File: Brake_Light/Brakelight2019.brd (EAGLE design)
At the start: 62.2 x 38.1 mm, 62 parts, among them J1 POWER_JACK, U1 R-78E5.0-1.0

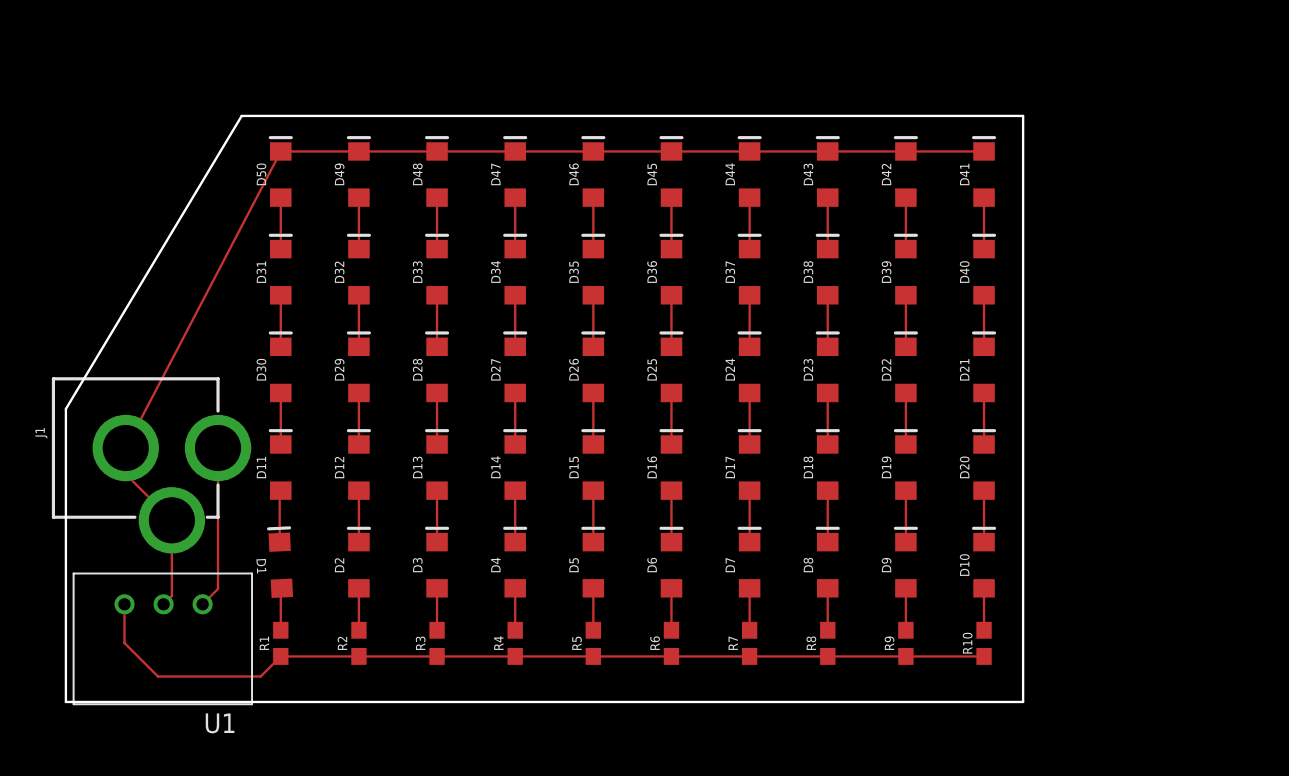
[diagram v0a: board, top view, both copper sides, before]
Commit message: Add files via upload
changed out LEDs and voltage regulator for better ones.
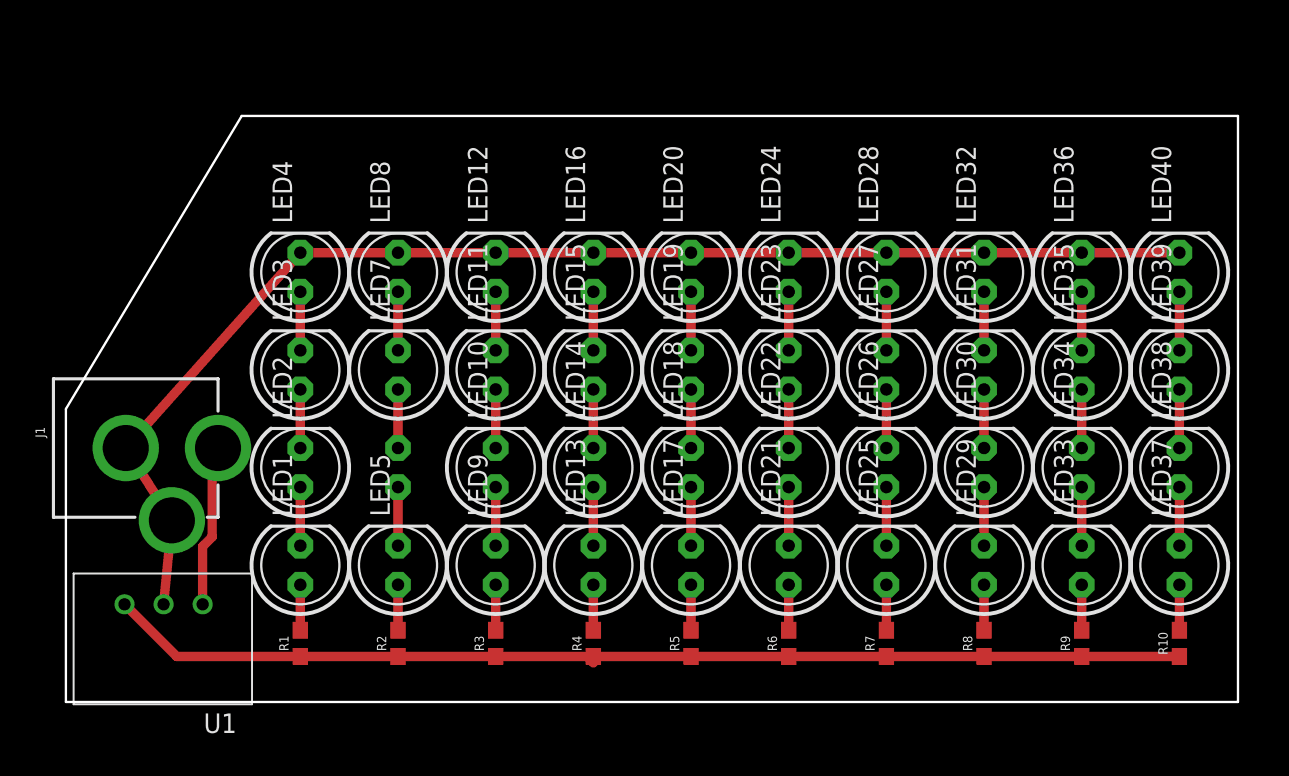
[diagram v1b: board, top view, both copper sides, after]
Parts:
- removed D1, D10, D11, D12, D13, D14, D15, D16, D17, D18, D19, D2, D20, D21, D22, D23, D24, D25, D26, D27, D28, D29, D3, D30, D31, D32, D33, D34, D35, D36, D37, D38, D39, D4, D40, D41, D42, D43, D44, D45, D46, D47, D48, D49, D5, D50, D6, D7, D8, D9: RED, SparkFun-LED:LED-1206
- added LED1, LED10, LED11, LED12, LED13, LED14, LED15, LED16, LED17, LED18, LED19, LED2, LED20, LED21, LED22, LED23, LED24, LED25, LED26, LED27, LED28, LED29, LED3, LED30, LED31, LED32, LED33, LED34, LED35, LED36, LED37, LED38, LED39, LED4, LED40, LED5, LED6, LED7, LED8, LED9: (no value), adafruit:LED5MM
- moved R10 12.7 mm to (77.5, 3.81)
- moved R9 11.4 mm to (71.1, 3.81)
- moved R8 10.2 mm to (64.8, 3.81)
- moved R7 8.89 mm to (58.4, 3.81)
- moved R6 7.62 mm to (52.1, 3.81)
- moved R5 6.35 mm to (45.7, 3.81)
- moved R4 5.08 mm to (39.4, 3.81)
- moved R3 3.81 mm to (33.0, 3.81)
- moved R2 2.54 mm to (26.7, 3.81)
- moved R1 1.27 mm to (20.3, 3.81)
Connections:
- removed net N$41: D1.A, R1.2
- removed net N$42: D2.A, R2.2
- removed net N$43: D3.A, R3.2
- removed net N$44: D4.A, R4.2
- removed net N$45: D5.A, R5.2
- removed net N$46: D6.A, R6.2
- removed net N$47: D7.A, R7.2
- removed net N$48: D8.A, R8.2
- removed net N$49: D9.A, R9.2
- removed net N$50: D10.A, R10.2
- net GND: now also LED12.K, LED16.K, LED20.K, LED24.K, LED28.K, LED32.K, LED36.K, LED4.K, LED40.K, LED8.K; no longer D41.C, D42.C, D43.C, D44.C, D45.C, D46.C, D47.C, D48.C, D49.C, D50.C
- net N$1: now also LED1.A, R1.2; no longer D1.C, D11.A
- net N$10: now also LED10.A, LED9.K; no longer D10.C, D20.A
- net N$11: now also LED10.K, LED11.A; no longer D20.C, D21.A
- net N$12: now also LED11.K, LED12.A; no longer D19.C, D22.A
- net N$13: now also LED13.A, R4.2; no longer D18.C, D23.A
- net N$14: now also LED13.K, LED14.A; no longer D17.C, D24.A
- net N$15: now also LED14.K, LED15.A; no longer D16.C, D25.A
- net N$16: now also LED15.K, LED16.A; no longer D15.C, D26.A
- net N$17: now also LED17.A, R5.2; no longer D14.C, D27.A
- net N$18: now also LED17.K, LED18.A; no longer D13.C, D28.A
- net N$19: now also LED18.K, LED19.A; no longer D12.C, D29.A
- net N$2: now also LED1.K, LED2.A; no longer D12.A, D2.C
- net N$20: now also LED19.K, LED20.A; no longer D11.C, D30.A
- net N$21: now also LED21.A, R6.2; no longer D30.C, D31.A
- net N$22: now also LED21.K, LED22.A; no longer D29.C, D32.A
- net N$23: now also LED22.K, LED23.A; no longer D28.C, D33.A
- net N$24: now also LED23.K, LED24.A; no longer D27.C, D34.A
- net N$25: now also LED25.A, R7.2; no longer D26.C, D35.A
- net N$26: now also LED25.K, LED26.A; no longer D25.C, D36.A
- net N$27: now also LED26.K, LED27.A; no longer D24.C, D37.A
- net N$28: now also LED27.K, LED28.A; no longer D23.C, D38.A
- net N$29: now also LED29.A, R8.2; no longer D22.C, D39.A
- net N$3: now also LED2.K, LED3.A; no longer D13.A, D3.C
- net N$30: now also LED29.K, LED30.A; no longer D21.C, D40.A
- net N$31: now also LED30.K, LED31.A; no longer D40.C, D41.A
- net N$32: now also LED31.K, LED32.A; no longer D39.C, D42.A
- net N$33: now also LED33.A, R9.2; no longer D38.C, D43.A
- net N$34: now also LED33.K, LED34.A; no longer D37.C, D44.A
- net N$35: now also LED34.K, LED35.A; no longer D36.C, D45.A
- net N$36: now also LED35.K, LED36.A; no longer D35.C, D46.A
- net N$37: now also LED37.A, R10.2; no longer D34.C, D47.A
- net N$38: now also LED37.K, LED38.A; no longer D33.C, D48.A
- net N$39: now also LED38.K, LED39.A; no longer D32.C, D49.A
- net N$4: now also LED3.K, LED4.A; no longer D14.A, D4.C
- net N$40: now also LED39.K, LED40.A; no longer D31.C, D50.A
- net N$5: now also LED5.A, R2.2; no longer D15.A, D5.C
- net N$6: now also LED5.K, LED6.A; no longer D16.A, D6.C
- net N$7: now also LED6.K, LED7.A; no longer D17.A, D7.C
- net N$8: now also LED7.K, LED8.A; no longer D18.A, D8.C
- net N$9: now also LED9.A, R3.2; no longer D19.A, D9.C
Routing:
- net 5V: track 59.8 -> 70.2 mm
- net GND: track 79.1 -> 85.2 mm
- net N$41: track 2.76 -> 0.00 mm
- net N$50: track 2.73 -> 0.00 mm
- net N$49: track 2.73 -> 0.00 mm
- net N$48: track 2.73 -> 0.00 mm
- net N$47: track 2.73 -> 0.00 mm
- net N$46: track 2.73 -> 0.00 mm
- net N$45: track 2.73 -> 0.00 mm
- net N$44: track 2.73 -> 0.00 mm
- net N$43: track 2.73 -> 0.00 mm
- net N$42: track 2.73 -> 0.00 mm
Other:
- board size 62.2 x 38.1 mm -> 76.2 x 38.1 mm

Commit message: Add files via upload
Here you go tony
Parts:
- added 5V_BYPASS: (no value), SparkFun-Connectors:1X02
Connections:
- net 5V: now also 5V_BYPASS.1
- net GND: now also 5V_BYPASS.2
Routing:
- net GND: track 85.2 -> 94.9 mm
- net 5V: track 70.2 -> 73.8 mm
- added copper zone on layer 1, net 5V
- added copper zone on layer 16, net GND
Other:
- board size 76.2 x 38.1 mm -> 77.5 x 33 mm
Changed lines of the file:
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@@
 <board>
 <plain>
-<wire x1="5.08" y1="0" x2="81.28" y2="0" width="0.1524" layer="20"/>
-<wire x1="81.28" y1="0" x2="81.28" y2="38.1" width="0.1524" layer="20"/>
-<wire x1="81.28" y1="38.1" x2="16.51" y2="38.1" width="0.1524" layer="20"/>
-<wire x1="16.51" y1="38.1" x2="5.08" y2="19.05" width="0.1524" layer="20"/>
+<wire x1="5.08" y1="0" x2="82.55" y2="0" width="0.1524" layer="20"/>
+<wire x1="82.55" y1="0" x2="82.55" y2="33.02" width="0.1524" layer="20"/>
+<wire x1="82.55" y1="33.02" x2="5.08" y2="33.02" width="0.1524" layer="20"/>
+<wire x1="5.08" y1="33.02" x2="5.08" y2="19.05" width="0.1524" layer="20"/>
 <wire x1="5.08" y1="19.05" x2="5.08" y2="0" width="0.1524" layer="20"/>
 <dimension x1="17.78" y1="31.75" x2="80.01" y2="40.64" x3="48.895" y3="41.91" textsize="1.778" layer="1" dtype="horizontal"/>
 <dimension x1="83.82" y1="30.48" x2="100.33" y2="6.35" x3="100.33" y3="18.415" textsize="1.778" layer="1" dtype="vertical"/>
+<hole x="6.858" y="31.496" drill="1"/>
+<hole x="15.24" y="31.496" drill="1"/>
+<hole x="6.858" y="22.86" drill="1"/>
+<hole x="81.28" y="1.27" drill="1"/>
+<hole x="6.35" y="1.27" drill="1"/>
+<hole x="41.91" y="1.016" drill="1"/>
+<hole x="81.28" y="31.75" drill="1"/>
+<hole x="41.91" y="31.75" drill="1"/>
+<hole x="60.96" y="31.75" drill="1"/>
+<hole x="60.96" y="1.016" drill="1"/>
+<hole x="28.194" y="31.75" drill="1"/>
+<hole x="28.448" y="1.016" drill="1"/>
+<hole x="81.28" y="17.78" drill="1"/>
 </plain>
 <attributes>
@@
 <element name="LED39" library="adafruit" library_urn="urn:adsk.eagle:library:420" package="LED5MM" package3d_urn="urn:adsk.eagle:package:6240538/1" value="" x="77.47" y="21.59" rot="R90"/>
 <element name="LED40" library="adafruit" library_urn="urn:adsk.eagle:library:420" package="LED5MM" package3d_urn="urn:adsk.eagle:package:6240538/1" value="" x="77.47" y="27.94" rot="R90"/>
+<element name="5V_BYPASS" library="SparkFun-Connectors" library_urn="urn:adsk.eagle:library:513" package="1X02" package3d_urn="urn:adsk.eagle:package:38039/1" value="" x="11.938" y="2.032" rot="R180"/>
 </elements>
 <signals>
@@
 <wire x1="20.32" y1="29.21" x2="8.97" y2="16.51" width="0.6096" layer="1"/>
 <wire x1="8.97" y1="16.51" x2="11.97" y2="11.81" width="0.6096" layer="1"/>
-<wire x1="11.97" y1="11.81" x2="11.43" y2="6.35" width="0.6096" layer="1"/>
+<wire x1="11.97" y1="11.81" x2="11.556846875" y2="7.632575" width="0.6096" layer="1"/>
+<contactref element="5V_BYPASS" pad="2"/>
+<wire x1="11.556846875" y1="7.632575" x2="11.43" y2="6.35" width="0.6096" layer="1"/>
+<wire x1="9.398" y1="2.032" x2="9.398" y2="2.22436875" width="0.6096" layer="1"/>
+<wire x1="9.398" y1="2.22436875" x2="7.708" y2="3.91436875" width="0.6096" layer="1"/>
+<wire x1="7.708" y1="3.91436875" x2="7.708" y2="6.739475" width="0.6096" layer="1"/>
+<wire x1="7.708" y1="6.739475" x2="8.429725" y2="7.4612" width="0.6096" layer="1"/>
+<wire x1="11.385471875" y1="7.4612" x2="11.556846875" y2="7.632575" width="0.6096" layer="1"/>
+<wire x1="8.429725" y1="7.4612" x2="11.385471875" y2="7.4612" width="0.6096" layer="1"/>
+<polygon width="0.6096" layer="16">
+<vertex x="5.08" y="33.02"/>
+<vertex x="5.08" y="0"/>
+<vertex x="82.55" y="0"/>
+<vertex x="82.55" y="33.02"/>
+</polygon>
 </signal>
 <signal name="5V">
@@
 <contactref element="R9" pad="1"/>
 <contactref element="R10" pad="1"/>
-<wire x1="20.32" y1="2.96" x2="12.28" y2="2.96" width="0.6096" layer="1"/>
-<wire x1="12.28" y1="2.96" x2="8.89" y2="6.35" width="0.6096" layer="1"/>
+<wire x1="19.05" y1="4.23" x2="12.192" y2="4.23" width="0.6096" layer="1"/>
+<wire x1="12.192" y1="4.23" x2="8.978" y2="4.23" width="0.6096" layer="1"/>
+<wire x1="8.978" y1="4.23" x2="8.89" y2="4.142" width="0.6096" layer="1"/>
 <wire x1="20.32" y1="2.96" x2="26.67" y2="2.96" width="0.6096" layer="1"/>
 <wire x1="26.67" y1="2.96" x2="33.02" y2="2.96" width="0.6096" layer="1"/>
@@
 <wire x1="64.77" y1="2.96" x2="71.12" y2="2.96" width="0.6096" layer="1"/>
 <wire x1="71.12" y1="2.96" x2="77.47" y2="2.96" width="0.6096" layer="1"/>
-<wire x1="38.95" y1="2.96" x2="39.37" y2="2.96" width="0" layer="19" extent="1-1"/>
+<contactref element="5V_BYPASS" pad="1"/>
+<wire x1="20.32" y1="2.96" x2="19.05" y2="4.23" width="0.6096" layer="1"/>
+<wire x1="8.89" y1="4.142" x2="8.89" y2="6.35" width="0.6096" layer="1"/>
+<wire x1="11.938" y1="2.032" x2="11.938" y2="3.976" width="0.6096" layer="1"/>
+<wire x1="11.938" y1="3.976" x2="12.192" y2="4.23" width="0.6096" layer="1"/>
+<polygon width="0.6096" layer="1">
+<vertex x="5.08" y="33.02"/>
+<vertex x="5.08" y="0"/>
+<vertex x="82.55" y="0"/>
+<vertex x="82.55" y="33.02"/>
+</polygon>
 </signal>
 <signal name="N$1">

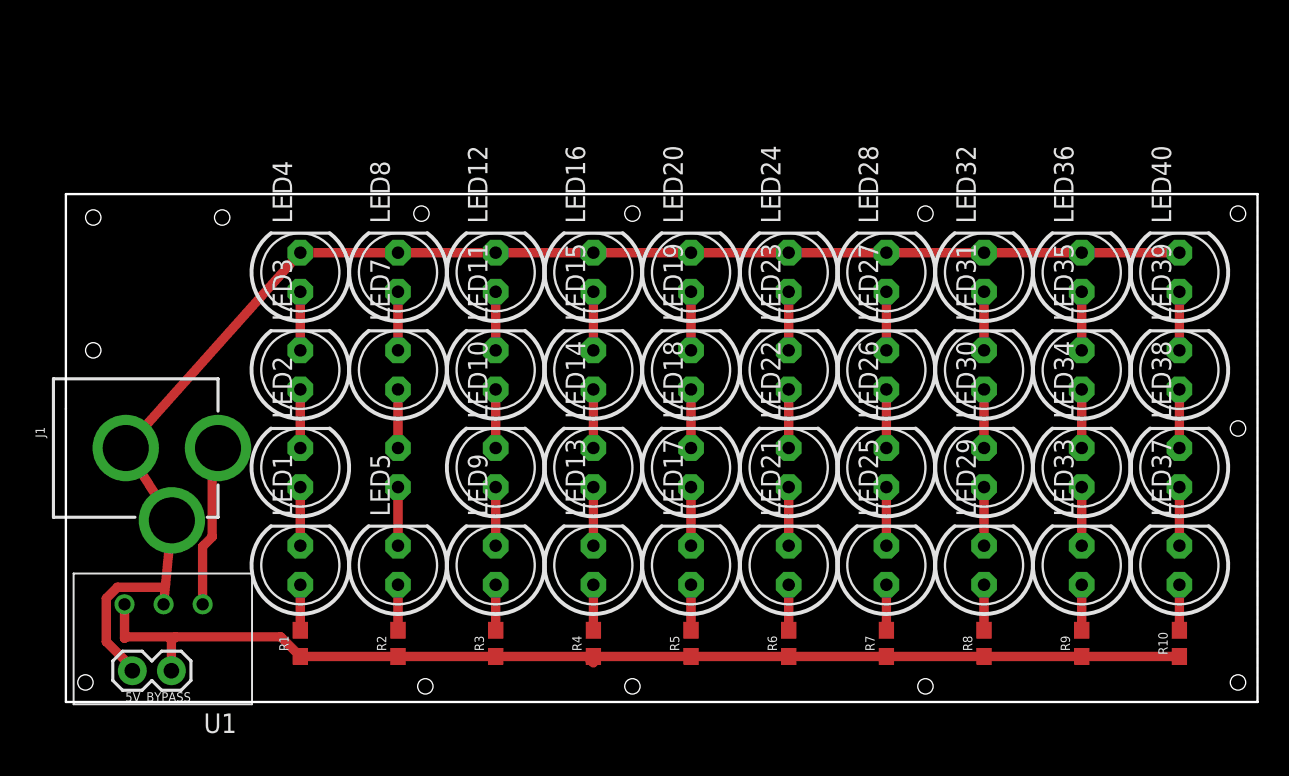
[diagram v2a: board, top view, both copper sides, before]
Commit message: Add files via upload
Changed LED configuration and removed 5V capability
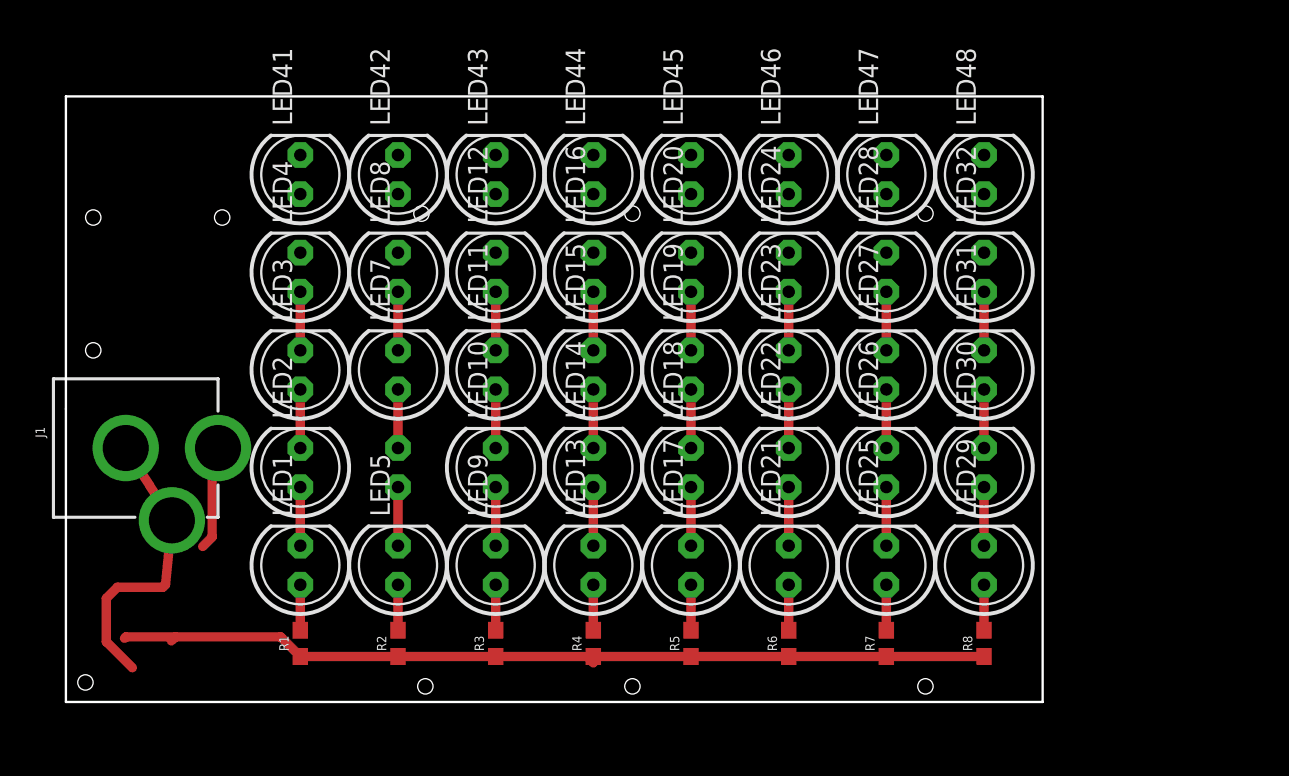
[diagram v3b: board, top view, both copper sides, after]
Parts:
- removed 5V_BYPASS: (no value), SparkFun-Connectors:1X02
- removed LED33, LED34, LED35, LED36, LED37, LED38, LED39, LED40: (no value), adafruit:LED5MM
- removed R10, R9: 330, SparkFun-Resistors:0603
- removed U1: R-78E5.0-1.0, SparkFun-IC-Power:DC-DC_CONVERTER_78XX
- added LED41, LED42, LED43, LED44, LED45, LED46, LED47, LED48: (no value), adafruit:LED5MM
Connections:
- removed net N$33: LED33.A, R9.2
- removed net N$34: LED33.K, LED34.A
- removed net N$35: LED34.K, LED35.A
- removed net N$36: LED35.K, LED36.A
- removed net N$37: LED37.A, R10.2
- removed net N$38: LED37.K, LED38.A
- removed net N$39: LED38.K, LED39.A
- removed net N$40: LED39.K, LED40.A
- new net N$41: LED4.K, LED41.A
- new net N$42: LED42.A, LED8.K
- new net N$43: LED12.K, LED43.A
- new net N$44: LED16.K, LED44.A
- new net N$45: LED20.K, LED45.A
- new net N$46: LED24.K, LED46.A
- new net N$47: LED28.K, LED47.A
- new net N$48: LED32.K, LED48.A
- net 12V: no longer U1.VIN
- net 5V: no longer 5V_BYPASS.1, R10.1, R9.1, U1.VOUT
- net GND: now also LED41.K, LED42.K, LED43.K, LED44.K, LED45.K, LED46.K, LED47.K, LED48.K; no longer 5V_BYPASS.2, LED12.K, LED16.K, LED20.K, LED24.K, LED28.K, LED32.K, LED36.K, LED4.K, LED40.K, LED8.K, U1.GND
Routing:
- net GND: track 94.9 -> 19.2 mm
- net 5V: track 73.8 -> 57.0 mm
- net N$40: track 3.81 -> 0.00 mm
- net N$36: track 3.81 -> 0.00 mm
- net N$38: track 3.81 -> 0.00 mm
- net N$34: track 3.81 -> 0.00 mm
- net N$39: track 3.81 -> 0.00 mm
- net N$35: track 3.81 -> 0.00 mm
- net 12V: track 10.6 -> 6.81 mm
- net N$37: track 2.96 -> 0.00 mm
- net N$33: track 2.96 -> 0.00 mm
- removed copper zone on layer 1, net 5V
- removed copper zone on layer 16, net GND
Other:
- board size 77.5 x 33 mm -> 63.5 x 39.4 mm
